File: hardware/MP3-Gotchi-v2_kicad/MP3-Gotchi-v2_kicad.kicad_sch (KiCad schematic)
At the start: 44 parts, among them IC1 SC189ZSKTRT, J1 Li-Ion, J3 112I-TA01, P1 USB_C_Plug_USB2.0, Q1 FS8205A, U1 ESP32-S3-WROOM, U2 TP4056-42-ESOP8, U3 DW01A, U4 LM4808M

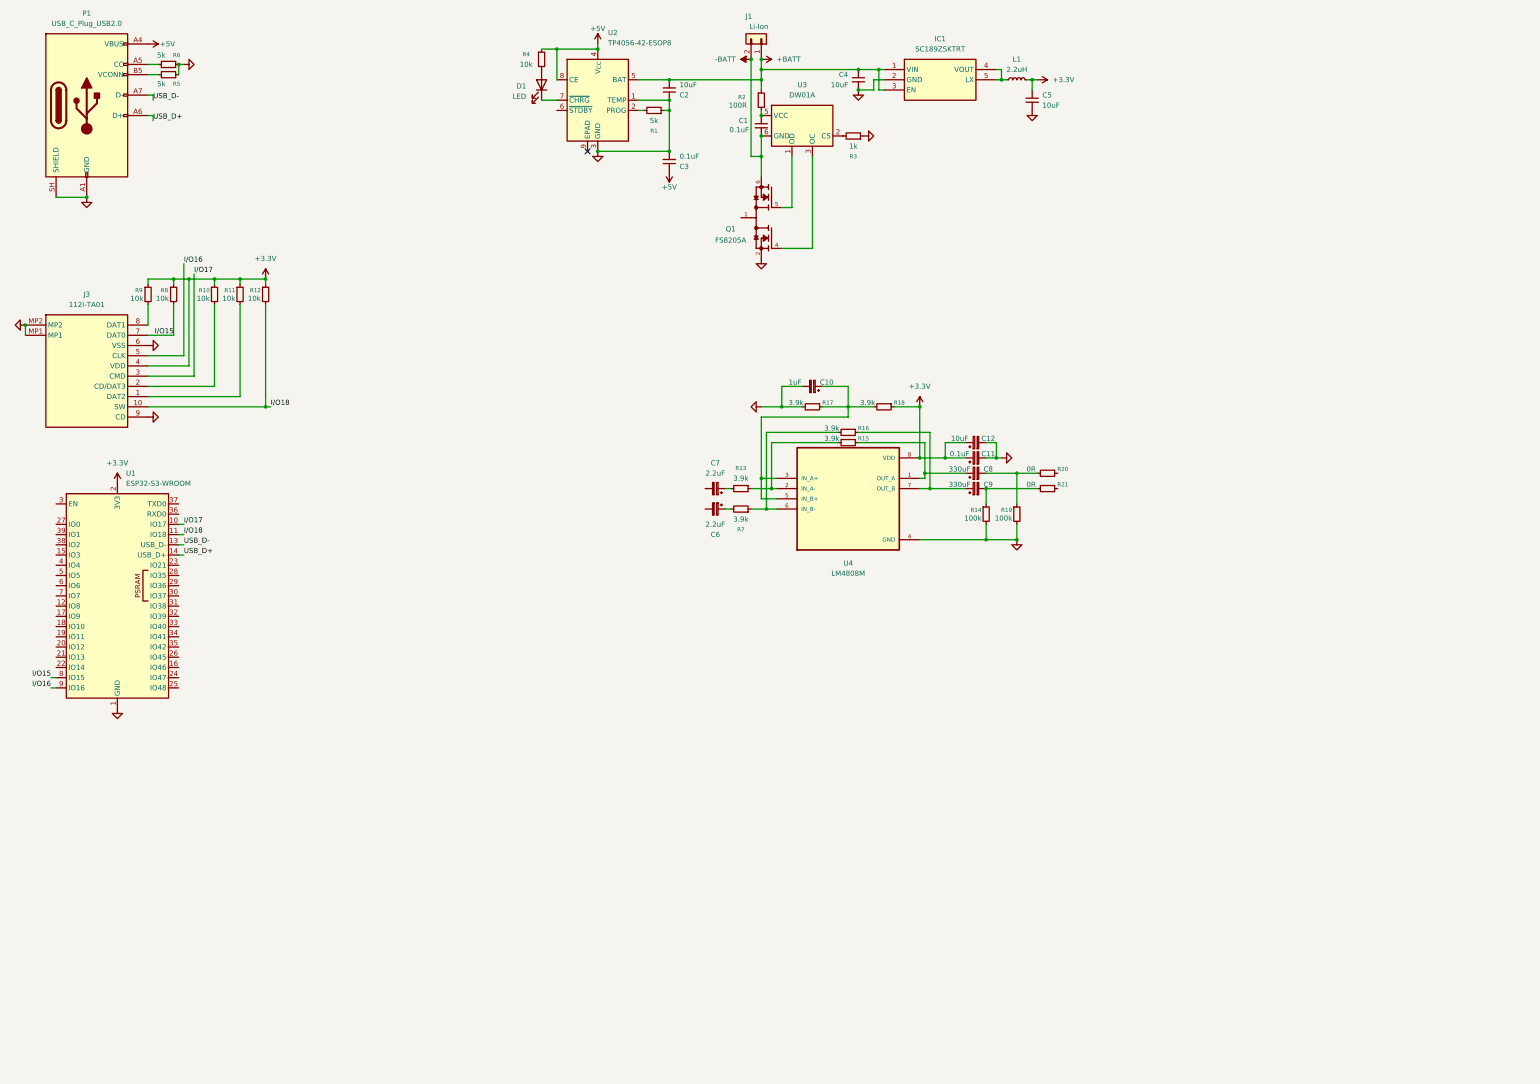
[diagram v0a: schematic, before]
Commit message: 0.0.2
Finished the TRRS jack, microphone input and most of the audio path. I chose the PCM5102A DAC and decided to reuse parts from dev boards instead of adding a full programmer circuit. The goal remains a small, clear and community-friendly MP3-Gotchi.
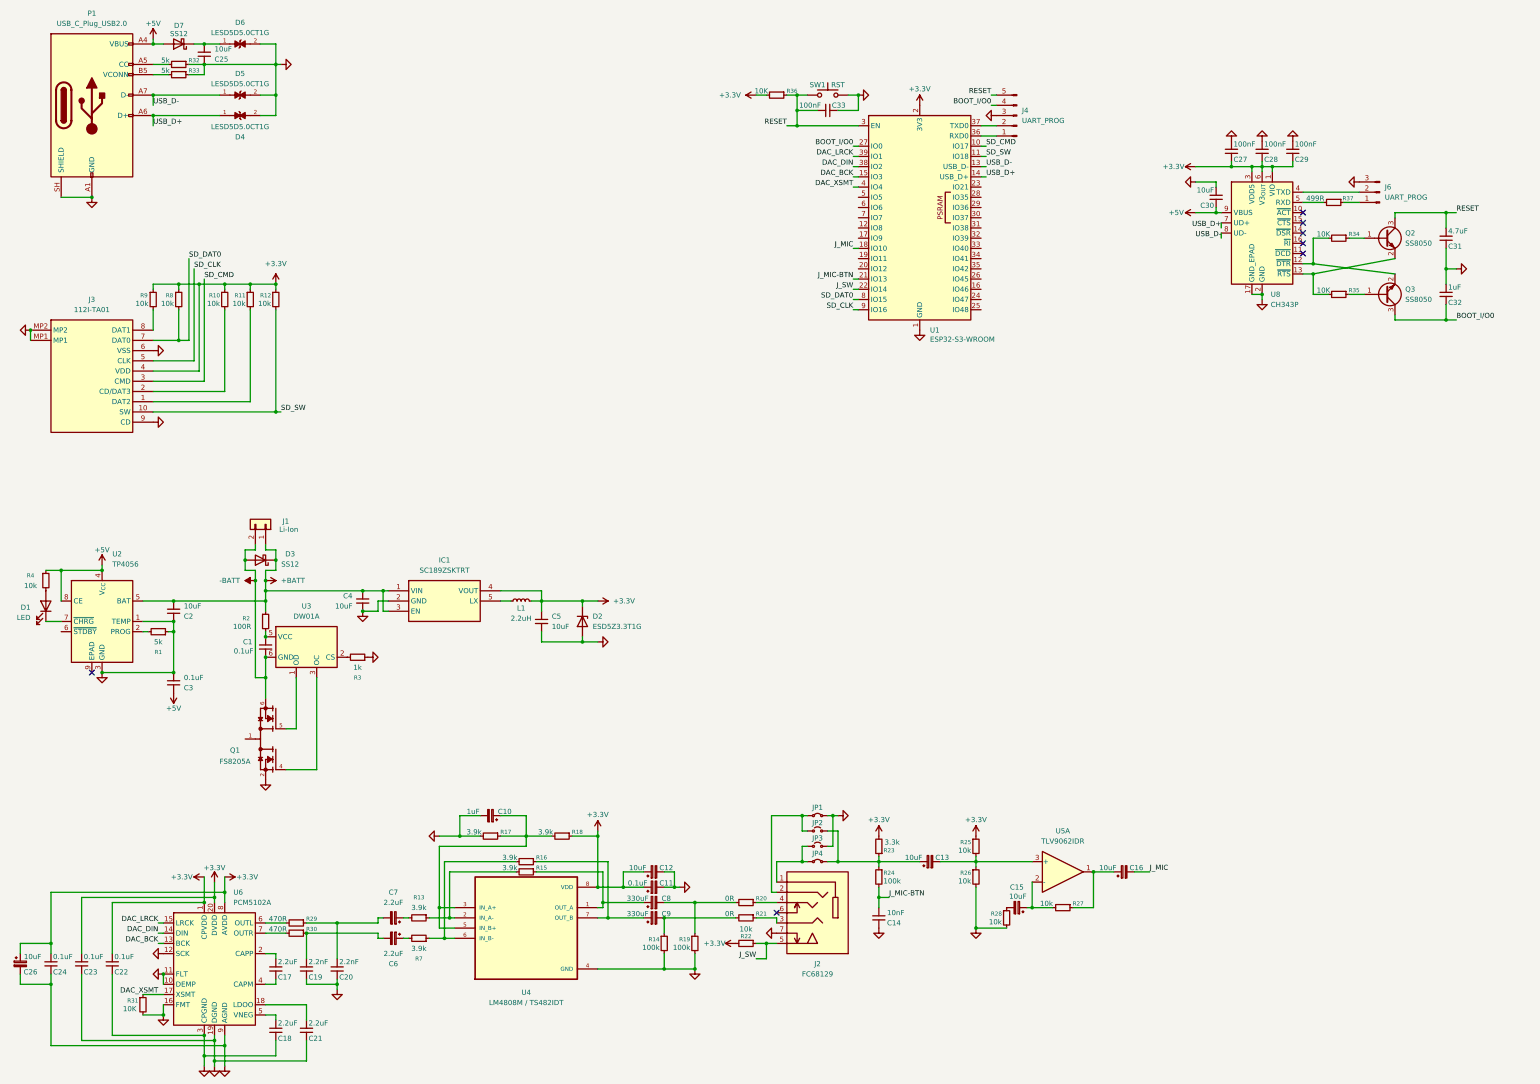
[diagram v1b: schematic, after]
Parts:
- removed R5, R6: 5k, symbol Device:R_Small
- added C13, C15, C16, C26: 10uF, symbol Device:C_Polarized_Small
- added C14: 10nF, symbol Device:C_Small
- added C17, C18, C21: 2.2uF, symbol Device:C_Small
- added C19, C20: 2.2nF, symbol Device:C_Small
- added C22, C23, C24: 0.1uF, symbol Device:C_Small
- added C25, C30: 10uF, symbol Device:C_Small
- added C27, C28, C29, C33: 100nF, symbol Device:C_Small
- added C31: 4.7uF, symbol Device:C_Small
- added C32: 1uF, symbol Device:C_Small
- added D2: ESD5Z3.3T1G, Diode_SMD:D_SOD-523, symbol Diode:ESD5Zxx
- added D3, D7: SS12, Diode_SMD:D_SMA, symbol Diode:SS12
- added D4, D5, D6: LESD5D5.0CT1G, LESD5D5.0CT1G:TVS_LESD5D5.0CT1G, symbol LESD5D5.0CT1G:LESD5D5.0CT1G
- added J2: FC68129, symbol FC68129_clean:FC68129
- added J4: UART_PROG, symbol Connector:Conn_01x05_Pin
- added J6: UART_PROG, symbol Connector:Conn_01x03_Pin
- added JP1, JP4: Jumper_2_Small_Bridged, symbol Jumper:Jumper_2_Small_Bridged
- added JP2, JP3: Jumper_2_Small_Open, symbol Jumper:Jumper_2_Small_Open
- added Q2, Q3: SS8050, Package_TO_SOT_SMD:SOT-23, symbol Transistor_BJT:SS8050
- added R22, R25, R26, R27, R28: 10k, symbol Device:R_Small
- added R23: 3.3k, symbol Device:R_Small
- added R24: 100k, symbol Device:R_Small
- added R29, R30: 470R, symbol Device:R_Small
- added R31, R34, R35, R36: 10K, symbol Device:R_Small
- added R32, R33: 5k, symbol Device:R_Small
- added R37: 499R, symbol Device:R_Small
- added SW1: RST, symbol Switch:SW_Push
- added U5: TLV9062IDR, Package_SO:SOIC-8_3.9x4.9mm_P1.27mm, symbol Amplifier_Operational:TLV9062xD
- added U6: PCM5102A, Package_SO:TSSOP-20_4.4x6.5mm_P0.65mm, symbol Audio:PCM5102A
- added U8: CH343P, Package_DFN_QFN:WCH_QFN-16-1EP_3x3mm_P0.5mm_EP1.8x1.8mm, symbol Interface_USB:CH343P
- U2: value TP4056-42-ESOP8 -> TP4056
- U4: value LM4808M -> LM4808M / TS482IDT
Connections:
- net +3.3V: now also IC1.4 (VOUT), C22.2, C23.2, C24.2, C26.1, C27.1, C28.1, C29.1, D2.1 (K), R22.2, R23.2, R25.1, R36.2, U6.1 (CPVDD), U6.20 (DVDD), U6.8 (AVDD), U8.1 (VIO), U8.3 (VDD5), U8.6 (V3_{OUT})
- net +5V: now also C30.1, D7.2 (A), U8.9 (VBUS)
- net +BATT: now also D3.1 (K)
- net -BATT: now also D3.2 (A)
- net GND: now also C14.1, C18.1, C19.1, C20.1, C21.1, C22.1, C23.1, C24.1, C25.1, C26.2, C27.2, C28.2, C29.2, C30.2, C31.1, C32.2, C33.1, D2.2 (A), D4.2, D5.2, D6.2, J2.7 (SW_B), J4.3 (Pin_3), J6.3 (Pin_3), JP1.2 (B), JP3.2 (B), R26.2, R28.2, R31.2, R32.1, R33.1, SW1.2, U6.10 (DEMP), U6.11 (FLT), U6.12 (SCK), U6.16 (FMT), U6.19 (DGND), U6.3 (CPGND), U6.9 (AGND), U8.17 (GND_EPAD), U8.2 (GND)
- net USB_D+: now also D4.1, U8.7 (UD+)
- net USB_D-: now also D5.1, U8.8 (UD-)
- net at IC1.5 (LX), L1.1: no longer IC1.4 (VOUT)
- net at P1.A5 (CC): now also R32.2
- net at P1.B5 (VCONN): now also R33.2
- net at R20.1: now also J2.4 (T)
- net DAC_BCK: now reaches U1.15 (IO3)
- net DAC_BCK: now also U6.13 (BCK)
- net J_MIC: now reaches U1.18 (IO10)
- net J_MIC: now also C16.2
- net J_MIC-BTN: now reaches U1.21 (IO13)
- net J_MIC-BTN: now also C14.2, R24.2
- net J_SW: now reaches U1.22 (IO14)
- net J_SW: now also J2.5 (SW_A), R22.1
- net BOOT_I/O0: now reaches U1.27 (IO0)
- net BOOT_I/O0: now also C32.1, J4.4 (Pin_4), Q3.3 (C)
- net RESET: now reaches U1.3 (EN)
- net RESET: now also C31.2, C33.2, J4.5 (Pin_5), Q2.3 (C), R36.1, SW1.1
- net at U1.36 (RXD0): now also J4.1 (Pin_1)
- net at U1.37 (TXD0): now also J4.2 (Pin_2)
- net DAC_DIN: now reaches U1.38 (IO2)
- net DAC_DIN: now also U6.14 (DIN)
- net DAC_LRCK: now reaches U1.39 (IO1)
- net DAC_LRCK: now also U6.15 (LRCK)
- net DAC_XSMT: now reaches U1.4 (IO4)
- net DAC_XSMT: now also R31.1, U6.17 (XSMT)
- net at C6.2: now also C19.2, R30.1
- net at R21.1: now also J2.3 (R2)
- net at C7.2: now also C20.2, R29.1
- net I/O15 renamed SD_DAT0
- net I/O16 renamed SD_CLK
- net I/O17 renamed SD_CMD
- net I/O18 renamed SD_SW
- new net: R29.2, U6.6 (OUTL)
- new net: J2.1 (S), JP3.1 (A), JP4.1 (A)
- new net: C13.1, JP2.2 (B), JP4.2 (B), R23.1, R24.1
- new net: Q2.1 (B), R34.1
- new net: Q2.2 (E), R35.2, U8.13 (~{RTS})
- new net: J2.2 (R1), JP1.1 (A), JP2.1 (A)
- new net: R30.2, U6.7 (OUTR)
- new net: C15.2, R28.1
- new net: J6.1 (Pin_1), R37.1
- new net: R37.2, U8.5 (RXD)
- new net: C21.2, U6.18 (LDOO)
- new net: C25.2, D6.1, D7.1 (K)
- new net: C16.1, R27.1, U5.1
- new net: C15.1, R27.2, U5.2 (-)
- new net: C13.2, R25.2, R26.1, U5.3 (+)
- new net: C18.2, U6.5 (VNEG)
- new net: C17.1, U6.4 (CAPM)
- new net: C17.2, U6.2 (CAPP)
- new net: Q3.2 (E), R34.2, U8.12 (~{DTR})
- new net: J6.2 (Pin_2), U8.4 (TXD)
- new net: Q3.1 (B), R35.1
- no-connect marks 1 -> 7
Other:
- moved on the sheet: C1, C10, C11, C12, C2, C3, C4, C5, C6, C7, C8, C9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

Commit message: 0.0.3
Made the hardware plan, added a rotary encoder and two MOSFET-controlled vibration motors, then audited yesterday’s schematic. I found issues in the PCM5102A section and rebuilt most of the microphone preamp after the Falstad simulation showed it was wrong.
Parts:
- removed C13, C15, C16: 10uF, symbol Device:C_Polarized_Small
- removed R26, R27, R28: 10k, symbol Device:R_Small
- added C16, C38, C40: 0.1uF, symbol Device:C_Small
- added C34, C35, C36: 10uF, symbol Device:C_Polarized_Small
- added C39: 47pF, symbol Device:C_Small
- added C41: 10nF, symbol Device:C_Small
- added C42, C43: 10uF, symbol Device:C_Small
- added C44: 4.7nF, symbol Device:C_Small
- added D8, D9: SS12, Diode_SMD:D_SMA, symbol Diode:SS12
- added M1, M2: Vibration-Motor, C0720B001F:XDCR_C0720B001F, symbol Vibration-Motor:C0720B001F
- added Q4, Q5: AO3400A, Package_TO_SOT_SMD:SOT-23, symbol Transistor_FET:AO3400A
- added R38, R43, R44, R47: 10k, symbol Device:R_Small
- added R39, R45: 20k, symbol Device:R_Small
- added R41: 10K, symbol Device:R_Small
- added R42, R48: 1k, symbol Device:R_Small
- added R46: 200k, symbol Device:R_Small
- added R5, R6: 100R, symbol Device:R_Small
- added SW2: RotaryEncoder-Switch-15mm, symbol Device:RotaryEncoder_Switch_MP
- added unit 2 of U5
- added unit 3 of U5
- C21: value 2.2uF -> 0.1uF
- C33: value 100nF -> 1uF
- C8, C9: value 330uF -> 680uF
- R13, R7: value 3.9k -> 22k
- R17, R18: value 3.9k -> 100k
- R23: value 3.3k -> 2.2k
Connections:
- net +3.3V: now also C35.1, C36.1, R38.1, R41.1, R47.1; no longer C26.1, R23.2, R25.1
- net DAC_BCK: now also U1.7 (IO7); no longer U1.15 (IO3)
- net DAC_DIN: now also U1.6 (IO6); no longer U1.38 (IO2)
- net DAC_LRCK: now also U1.5 (IO5); no longer U1.39 (IO1)
- net DAC_XSMT: now also U1.12 (IO8); no longer U1.4 (IO4)
- net GND: now also R25.1, C34.2, C35.2, C36.2, C41.1, C42.2, C43.2, C44.2, Q4.2 (S), Q5.2 (S), R39.2, R43.2, R44.2, SW2.C, SW2.MP, SW2.S2; no longer C26.2
- net J_MIC: now also C44.1, R42.1
- net at JP2.2 (B), JP4.2 (B), R23.1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: now also C40.2
- net at C21.2, U6.18 (LDOO): now also C34.1
- net at U5.1: now also C39.1, R42.2, R46.1
- net at U5.2 (-): now also C39.2, R45.1, R46.2
- net at R25.2, U5.3 (+): now also C41.2, R47.2
- new net: C38.1, D9.1 (K), M2.1 (V+)
- new net: C38.2, D9.2 (A), M2.2 (V-), Q5.3 (D)
- new net: C40.1, R45.2
- new net: C43.1, R38.2, R39.1, U5.5 (+)
- new net: R48.1, U5.6 (-), U5.7
- new net: Q4.1 (G), R43.1, R5.1
- new net: Q5.1 (G), R44.1, R6.1
- new net: C42.1, R23.2, R48.2
- new net: C16.1, D8.1 (K), M1.1 (V+)
- new net: C16.2, D8.2 (A), M1.2 (V-), Q4.3 (D)
- new net ENC_A: SW2.A
- new net ENC_B: SW2.B
- new net ENC_SW: R41.2, SW2.S1
- new net MOT_1: R5.2
- new net MOT_2: R6.2
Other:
- moved on the sheet: C10, C11, C12, C14, C17, C18, C19, C20, C21, C22, C23, C24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

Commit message: 0.0.4
The schematic is nearly finished. I added the MPU6050, moved the SSD1331 to a separate PH-connected board, added a small speaker using the jack shunt and PAM8302 amplifier, and included two extra buttons. Only the usual PCB fixes remain.
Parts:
- added C37, C46, C49: 2.2nF, symbol Device:C_Small
- added C45: 0.1uF, symbol Device:C_Small
- added C47: 10nF, symbol Device:C_Small
- added C48: 1uF, symbol Device:C_Small
- added J5: OLED-SSD1331-SPI, symbol Connector_Generic:Conn_01x07
- added J7: Internal Speaker, symbol Connector_Generic:Conn_01x02
- added R26, R27: 4.7k, symbol Device:R_Small
- added R28, R50, R51: 10k, symbol Device:R_Small
- added R40, R49: 20k, symbol Device:R_Small
- added SW3: A, symbol Switch:SW_Push
- added SW4: B, symbol Switch:SW_Push
- added U7: MPU-6050, Sensor_Motion:InvenSense_QFN-24_4x4mm_P0.5mm, symbol Sensor_Motion:MPU-6050
- added U9: PAM8302AAD, symbol Amplifier_Audio:PAM8302AAD
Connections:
- net +3.3V: now also U5.8 (V+), C48.1, J5.VCC (Pin_2), R26.1, R27.1, R28.1, R50.2, U7.13 (VDD), U9.6 (VDD)
- net DAC_BCK: now also U1.6 (IO6); no longer U1.7 (IO7)
- net DAC_DIN: now also U1.5 (IO5); no longer U1.6 (IO6)
- net DAC_LRCK: now also U1.4 (IO4); no longer U1.5 (IO5)
- net DAC_XSMT: now also U1.7 (IO7); no longer U1.12 (IO8)
- net GND: now also U5.4 (V-), C37.1, C45.2, C46.2, C47.1, C48.2, C49.1, J5.GND (Pin_1), R49.2, SW3.1, SW4.1, U7.1 (CLKIN), U7.11 (FSYNC), U7.18 (GND), U7.9 (AD0), U9.7 (GND)
- net J_MIC: now also U1.31 (IO38); no longer U1.18 (IO10)
- net MPU_SDA: now reaches U1.17 (IO9)
- net MPU_SDA: now also R27.2, U7.24 (SDA)
- net DISP_MOSI: now reaches U1.19 (IO11)
- net DISP_MOSI: now also J5.MOSI (Pin_4)
- net DISP_CLK: now reaches U1.20 (IO12)
- net DISP_CLK: now also J5.CLK (Pin_3)
- net DISP_RES: now reaches U1.32 (IO39)
- net DISP_RES: now also J5.RES (Pin_5)
- net DISP_DC: now reaches U1.38 (IO2)
- net DISP_DC: now also J5.DC (Pin_6)
- net DISP_CS: now reaches U1.39 (IO1)
- net DISP_CS: now also J5.CS (Pin_7), R28.2
- net J_TS: now reaches J2.6 (T_SW)
- net J_TS: now also R40.2
- new net: C46.1, U7.20 (CPOUT)
- new net: C45.1, U7.10 (REGOUT)
- new net: C47.2, U7.8 (VLOGIC)
- new net: C37.2, J7.- (Pin_1), U9.8 (OUT-)
- new net: R40.1, U9.3 (IN+)
- new net: R49.1, U9.4 (IN-)
- new net: C49.2, J7.+ (Pin_2), U9.5 (OUT+)
- new net MPU_INT: U1.18 (IO10), U7.12 (INT)
- new net MPU_SCL: R26.2, U1.12 (IO8), U7.23 (SCL)
- new net SW_A: R50.1, R51.2, SW3.2
- new net SW_B: R51.1, SW4.2
- no-connect marks 7 -> 10
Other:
- moved on the sheet: C1, C10, C11, C12, C14, C16, C17, C18, C19, C2, C20, C21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
